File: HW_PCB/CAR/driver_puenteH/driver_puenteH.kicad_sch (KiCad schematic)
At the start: 6 parts, among them IC1 TB6612FNG, J3 Puente H, J4 Puente_H2

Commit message: Añadi nuevo proyecto del puente-H
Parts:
- C1_Driver1: renamed from C1_Driver; footprint (none) -> Capacitor_SMD:C_0805_2012Metric
- C2_driver1: renamed from C2_driver; footprint (none) -> Capacitor_SMD:C_0805_2012Metric
- C3_driver1: renamed from C3_driver; footprint (none) -> Capacitor_SMD:C_0805_2012Metric
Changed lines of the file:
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@@
 		(dnp no)
 		(fields_autoplaced yes)
-		(property "Reference" "C2_driver"
+		(property "Reference" "C2_driver1"
 			(at 152.4 48.2599 0)
 			(effects
@@
 			)
 		)
-		(property "Footprint" ""
+		(property "Footprint" "Capacitor_SMD:C_0805_2012Metric"
 			(at 149.5552 53.34 0)
 			(effects
@@
 			(project "driver_puenteH"
 				(path "/b3b63d40-911d-4ea6-b805-39f1fc607e60"
-					(reference "C2_driver")
+					(reference "C2_driver1")
 					(unit 1)
 				)
@@
 		(dnp no)
 		(fields_autoplaced yes)
-		(property "Reference" "C3_driver"
+		(property "Reference" "C3_driver1"
 			(at 95.25 40.6399 0)
 			(effects
@@
 			)
 		)
-		(property "Footprint" ""
+		(property "Footprint" "Capacitor_SMD:C_0805_2012Metric"
 			(at 92.4052 45.72 0)
 			(effects
@@
 			(project "driver_puenteH"
 				(path "/b3b63d40-911d-4ea6-b805-39f1fc607e60"
-					(reference "C3_driver")
+					(reference "C3_driver1")
 					(unit 1)
 				)
@@
 		(dnp no)
 		(fields_autoplaced yes)
-		(property "Reference" "C1_Driver"
+		(property "Reference" "C1_Driver1"
 			(at 78.74 40.6399 0)
 			(effects
@@
 			)
 		)
-		(property "Footprint" ""
+		(property "Footprint" "Capacitor_SMD:C_0805_2012Metric"
 			(at 75.8952 45.72 0)
 			(effects
@@
 			(project ""
 				(path "/b3b63d40-911d-4ea6-b805-39f1fc607e60"
-					(reference "C1_Driver")
-					(unit 1)
-				)
+					(reference "C1_Driver1")
+					(unit 1)
+				)

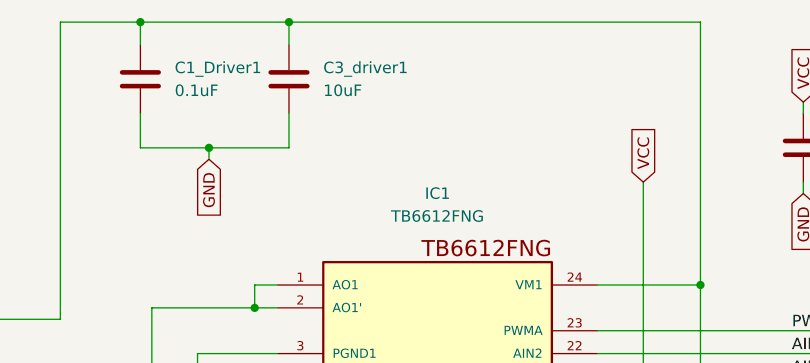
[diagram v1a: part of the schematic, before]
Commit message: Driver test Finalizado
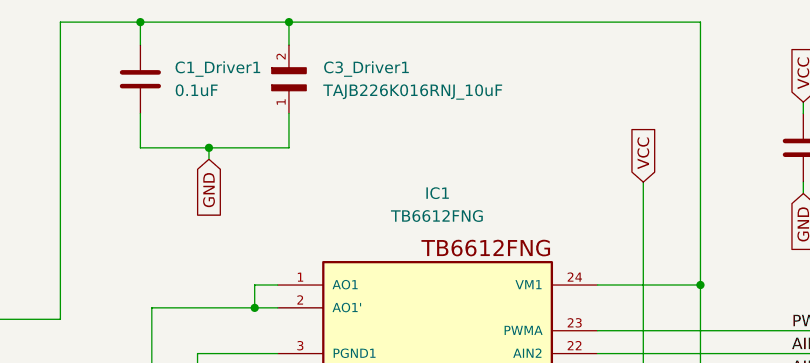
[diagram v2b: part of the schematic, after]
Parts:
- removed C3_driver1: 10uF, Capacitor_SMD:C_0805_2012Metric, symbol Device:C
- added C3_Driver1: TAJB226K016RNJ_10uF, TAJB226K016RNJ:CAPPC3528X210N, symbol TAJB226K016RNJ:TAJB226K016RNJ
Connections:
- net GND: now also C3_Driver1.1
- net VM: now also C3_Driver1.2
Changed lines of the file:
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@@
-	(symbol
-		(lib_id "Device:C")
-		(at 91.44 41.91 0)
-		(unit 1)
-		(exclude_from_sim no)
-		(in_bom yes)
-		(on_board yes)
-		(dnp no)
-		(fields_autoplaced yes)
-		(property "Reference" "C3_driver1"
-			(at 95.25 40.6399 0)
-			(effects
-				(font
-					(size 1.27 1.27)
-				)
-				(justify left)
-			)
-		)
-		(property "Value" "10uF"
-			(at 95.25 43.1799 0)
-			(effects
-				(font
-					(size 1.27 1.27)
-				)
-				(justify left)
-			)
-		)
-		(property "Footprint" "Capacitor_SMD:C_0805_2012Metric"
-			(at 92.4052 45.72 0)
-			(effects
-				(font
-					(size 1.27 1.27)
-				)
-				(hide yes)
-			)
-		)
-		(property "Datasheet" "~"
-			(at 91.44 41.91 0)
-			(effects
-				(font
-					(size 1.27 1.27)
-				)
-				(hide yes)
-			)
-		)
-		(property "Description" "Unpolarized capacitor"
-			(at 91.44 41.91 0)
-			(effects
-				(font
-					(size 1.27 1.27)
-				)
-				(hide yes)
-			)
-		)
-		(pin "2"
-		)
-		(pin "1"
-		)
-		(instances
-			(project "driver_puenteH"
-				(path "/b3b63d40-911d-4ea6-b805-39f1fc607e60"
-					(reference "C3_driver1")
-					(unit 1)
-				)
-			)
-		)
-	)
 	(symbol
 		(lib_id "Device:C")
@@
 					(unit 1)
 				)
+			)
+		)
+	)
+	(symbol
+		(lib_id "TAJB226K016RNJ:TAJB226K016RNJ")
+		(at 91.44 40.64 270)
+		(unit 1)
+		(exclude_from_sim no)
+		(in_bom yes)
+		(on_board yes)
+		(dnp no)
+		(fields_autoplaced yes)
+		(property "Reference" "C3_Driver1"
+			(at 95.25 40.6399 90)
+			(effects
+				(font
+					(size 1.27 1.27)
+				)
+				(justify left)
+			)
+		)
+		(property "Value" "TAJB226K016RNJ_10uF"
+			(at 95.25 43.1799 90)
+			(effects
+				(font
+					(size 1.27 1.27)
+				)
+				(justify left)
+			)
+		)
+		(property "Footprint" "TAJB226K016RNJ:CAPPC3528X210N"
+			(at 91.44 40.64 0)
+			(effects
+				(font
+					(size 1.27 1.27)
+				)
+				(justify bottom)
+				(hide yes)
+			)
+		)
+		(property "Datasheet" ""
+			(at 91.44 40.64 0)
+			(effects
+				(font
+					(size 1.27 1.27)
+				)
+				(hide yes)
+			)
+		)
+		(property "Description" ""
+			(at 91.44 40.64 0)
+			(effects
+				(font
+					(size 1.27 1.27)
+				)
+				(hide yes)
+			)
+		)
+		(property "DigiKey_Part_Number" "478-1682-1-ND"
+			(at 91.44 40.64 0)
+			(effects
+				(font
+					(size 1.27 1.27)
+				)
+				(justify bottom)
+				(hide yes)
+			)
+		)
+		(property "SnapEDA_Link" "https://www.snapeda.com/parts/TAJB226K016RNJ/AVX/view-part/?ref=snap"
+			(at 91.44 40.64 0)
+			(effects
+				(font
+					(size 1.27 1.27)
+				)
+				(justify bottom)
+				(hide yes)
+			)
+		)
+		(property "Description_1" "Capacitor, Tantalum, 22 uF, 16 V @ 85C, 20 V @ 85C, +/-10%, B, SMD, 6 % | AVX TAJB226K016RNJ"
+			(at 91.44 40.64 0)
+			(effects
+				(font
+					(size 1.27 1.27)
+				)
+				(justify bottom)
+				(hide yes)
+			)
+		)
+		(property "MF" "AVX"
+			(at 91.44 40.64 0)
+			(effects
+				(font
+					(size 1.27 1.27)
+				)
+				(justify bottom)
+				(hide yes)
+			)
+		)
+		(property "Package" "1210 AVX"
+			(at 91.44 40.64 0)
+			(effects
+				(font
+					(size 1.27 1.27)
+				)
+				(justify bottom)
+				(hide yes)
+			)
+		)
+		(property "Check_prices" "https://www.snapeda.com/parts/TAJB226K016RNJ/AVX/view-part/?ref=eda"
+			(at 91.44 40.64 0)
+			(effects
+				(font
+					(size 1.27 1.27)
+				)
+				(justify bottom)
+				(hide yes)
+			)
+		)
+		(property "MP" "TAJB226K016RNJ"
+			(at 91.44 40.64 0)
+			(effects
+				(font
+					(size 1.27 1.27)
+				)
+				(justify bottom)
+				(hide yes)
+			)
+		)
+		(pin "1"
+		)
+		(pin "2"
+		)
+		(instances
+			(project ""
+				(path "/b3b63d40-911d-4ea6-b805-39f1fc607e60"
+					(reference "C3_Driver1")
+					(unit 1)
+				)
